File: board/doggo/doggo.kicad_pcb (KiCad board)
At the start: 2 copper layers, 98.1 x 97.5 mm, 165 parts, among them U1 IS31FL3731, U2 LIS2HH12, U3 STM32F042K6, U4 MCP1640

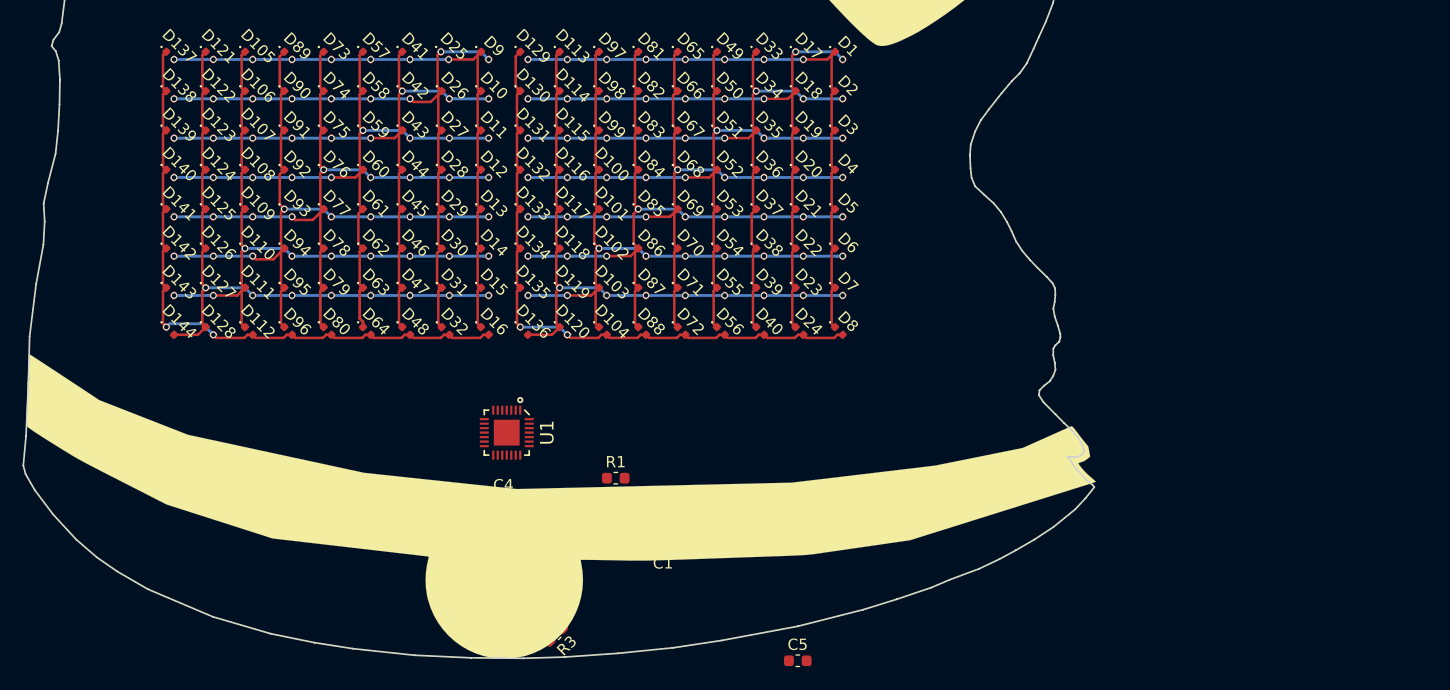
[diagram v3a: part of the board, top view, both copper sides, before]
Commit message: got all the footprints on the board
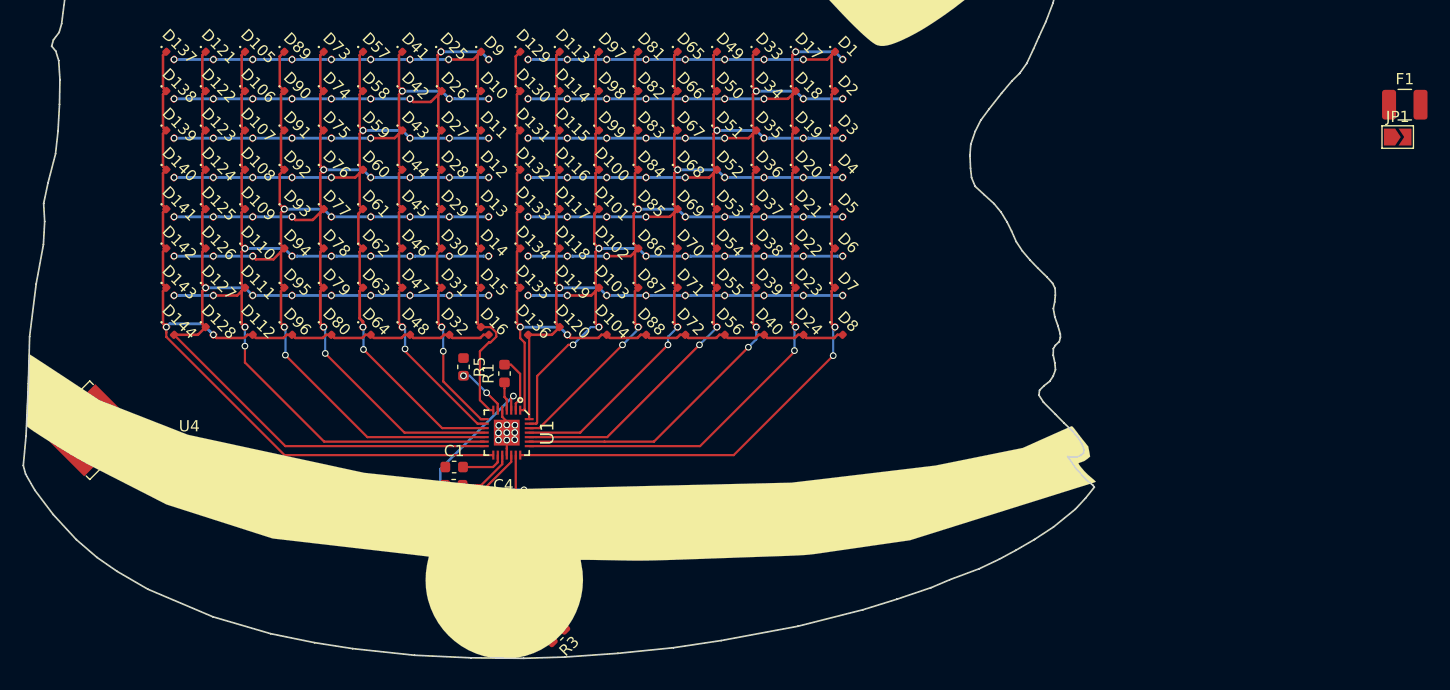
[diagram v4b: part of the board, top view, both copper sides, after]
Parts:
- added C7: 10uF, Capacitor_Tantalum_SMD:CP_EIA-3216-10_Kemet-I, F.Cu at (110.8, 128.6)
- added C8: 4.7uF, Capacitor_Tantalum_SMD:CP_EIA-3216-10_Kemet-I, F.Cu at (101.9, 127.7)
- added F1: Polyfuse, Fuse:Fuse_1210_3225Metric, F.Cu at (209.6, 93.1)
- added JP1: Jumper_2_Open, Jumper:SolderJumper-2_P1.3mm_Open_TrianglePad1.0x1.5mm, F.Cu at (209.0, 96.0)
- added L1: 4.7uH, Inductor_SMD:L_Bourns_SRN6045TA, F.Cu at (92.6, 122.1)
- moved C5 34.4 mm to (125.0, 127.0), turned to 180 degrees
- moved R5 25.6 mm to (125.8, 116.5), turned to 270 degrees
- moved R4 23.2 mm to (123.2, 131.8), turned to 315 degrees
- moved C1 19.9 mm to (125.0, 125.4), turned to 0 degrees
- moved R1 13.6 mm to (129.5, 117.0), turned to 90 degrees
- moved U4 2.11 mm to (101.5, 124.6)
- moved R2 0.80 mm to (134.2, 130.5)
- moved R6 0.34 mm to (124.7, 130.5)
- moved R3 0.20 mm to (134.2, 140.3)
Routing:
- net /SDA: track 0.00 -> 42.0 mm, vias 0 -> 2
- net +3V3: track 0.50 -> 41.1 mm, vias 0 -> 2
- net /CB9: track 57.1 -> 91.4 mm
- net /CA1: track 53.9 -> 88.0 mm, vias 8 -> 10
- net /CB8: track 54.8 -> 86.5 mm
- net /CA2: track 54.8 -> 84.1 mm, vias 9 -> 11
- net /CB7: track 54.8 -> 82.2 mm, vias 9 -> 11
- net /SCL: track 0.00 -> 27.0 mm
- net /CA3: track 54.9 -> 79.9 mm, vias 9 -> 11
- net /CB6: track 54.8 -> 78.0 mm, vias 9 -> 11
- net /CA4: track 54.8 -> 75.6 mm, vias 9 -> 11
- net /SDB: track 0.00 -> 20.0 mm, vias 0 -> 2
- net /CB5: track 54.6 -> 74.1 mm, vias 9 -> 11
- net /CA5: track 54.9 -> 72.4 mm, vias 9 -> 11
- net /CB4: track 54.9 -> 70.5 mm, vias 9 -> 11
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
